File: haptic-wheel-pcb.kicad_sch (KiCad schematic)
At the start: 2 parts, among them J1 Screw_Terminal_01x02, J2 Screw_Terminal_01x02

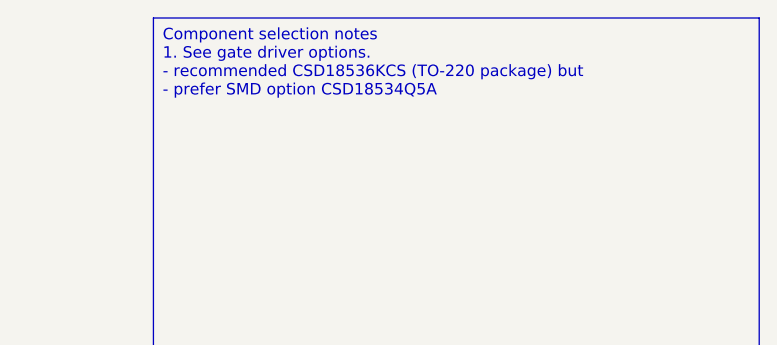
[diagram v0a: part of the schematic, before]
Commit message: routed motor driver fets and shunts
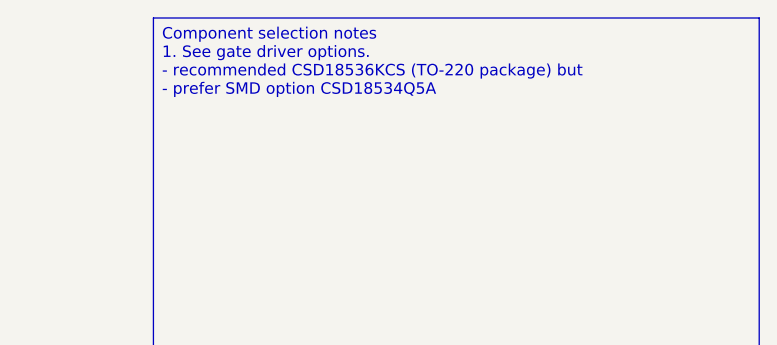
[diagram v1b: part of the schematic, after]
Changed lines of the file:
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@@
 (kicad_sch
-	(version 20231120)
+	(version 20250114)
 	(generator "eeschema")
-	(generator_version "8.0")
+	(generator_version "9.0")
 	(paper "A4")
 	(text_box "Component selection notes\n1. See gate driver options. \n  - recommended CSD18536KCS (TO-220 package) but \n  - prefer SMD option CSD18534Q5A\n"
@@
 		(at 308.61 15.24 0)
 		(size 67.31 44.45)
+		(margins 0.9525 0.9525 0.9525 0.9525)
 		(stroke
 			(width 0)
@@
 		(at 0 434.34)
 		(size 297.18 173.99)
+		(exclude_from_sim no)
+		(in_bom yes)
+		(on_board yes)
+		(dnp no)
 		(fields_autoplaced yes)
 		(stroke
@@
 		(at -2.54 642.62)
 		(size 298.45 233.68)
+		(exclude_from_sim no)
+		(in_bom yes)
+		(on_board yes)
+		(dnp no)
 		(fields_autoplaced yes)
 		(stroke
@@
 		(at -1.27 228.6)
 		(size 299.72 180.34)
+		(exclude_from_sim no)
+		(in_bom yes)
+		(on_board yes)
+		(dnp no)
 		(fields_autoplaced yes)
 		(stroke
@@
 		)
 	)
+	(embedded_fonts no)
 )

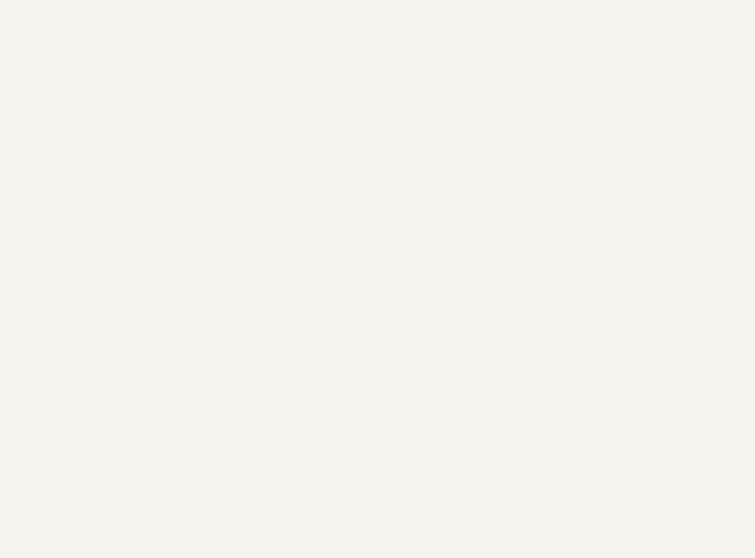
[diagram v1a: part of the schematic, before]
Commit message: route all 3 fets with shunts in a vertical line
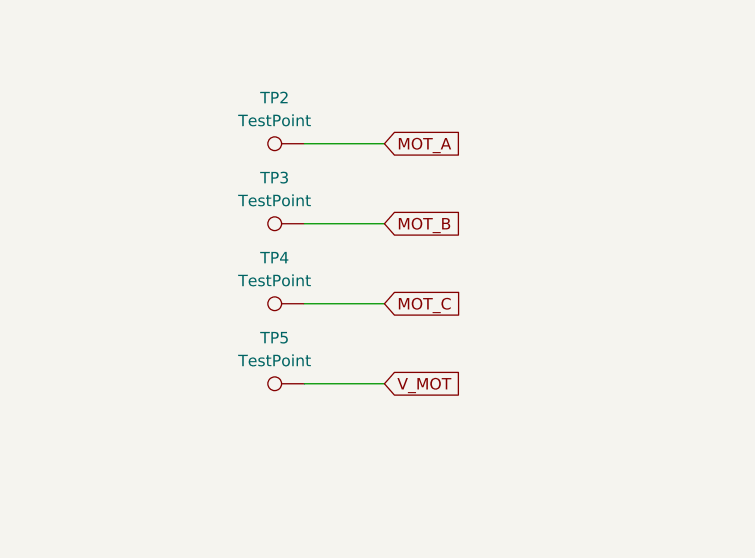
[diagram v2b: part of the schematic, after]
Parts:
- added TP2, TP3, TP4, TP5: TestPoint, TestPoint:TestPoint_Keystone_5019_Miniature, symbol Connector:TestPoint
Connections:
- new net MOT_A: TP2.1
- new net MOT_B: TP3.1
- new net MOT_C: TP4.1
- new net V_MOT: TP5.1

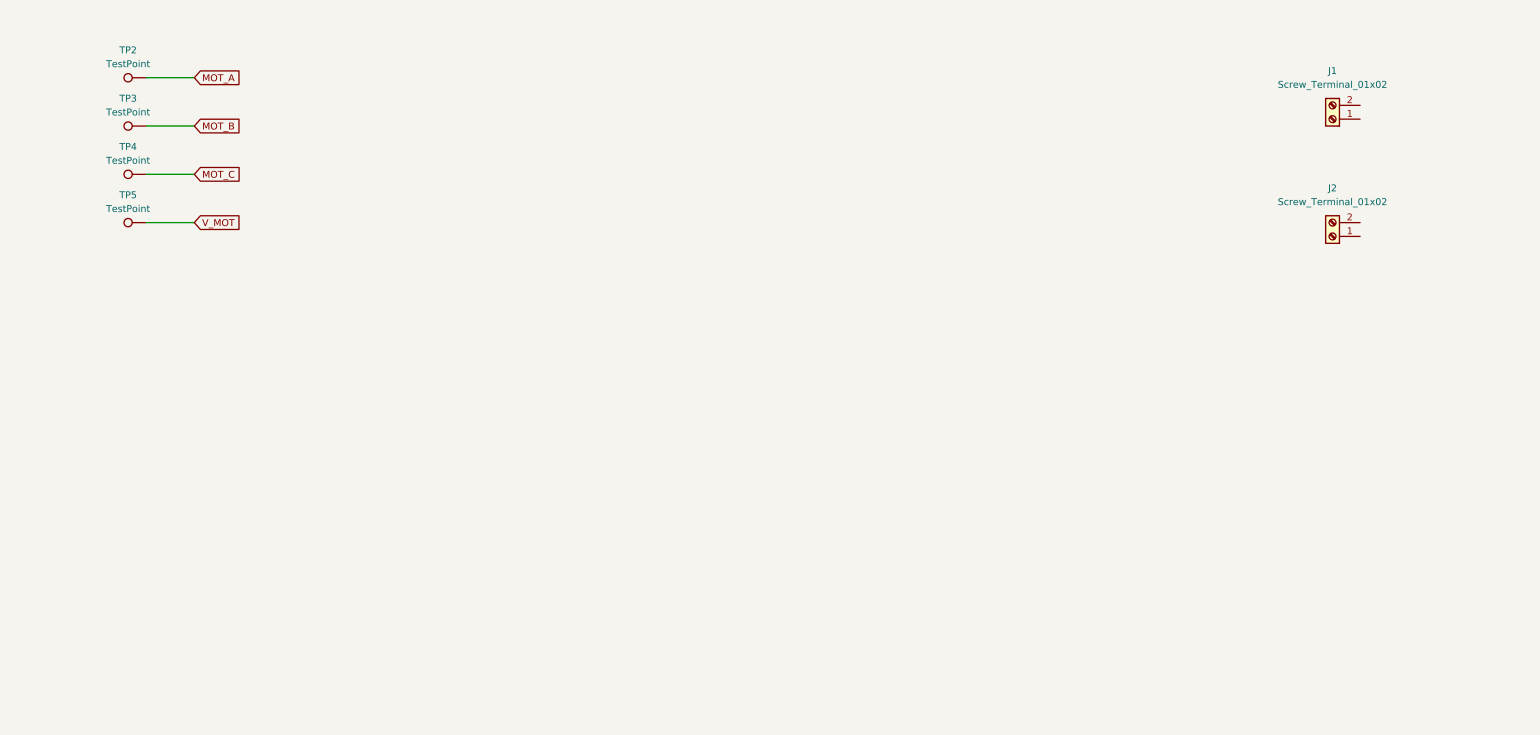
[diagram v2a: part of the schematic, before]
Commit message: selected mcu pins for sense in, SPI
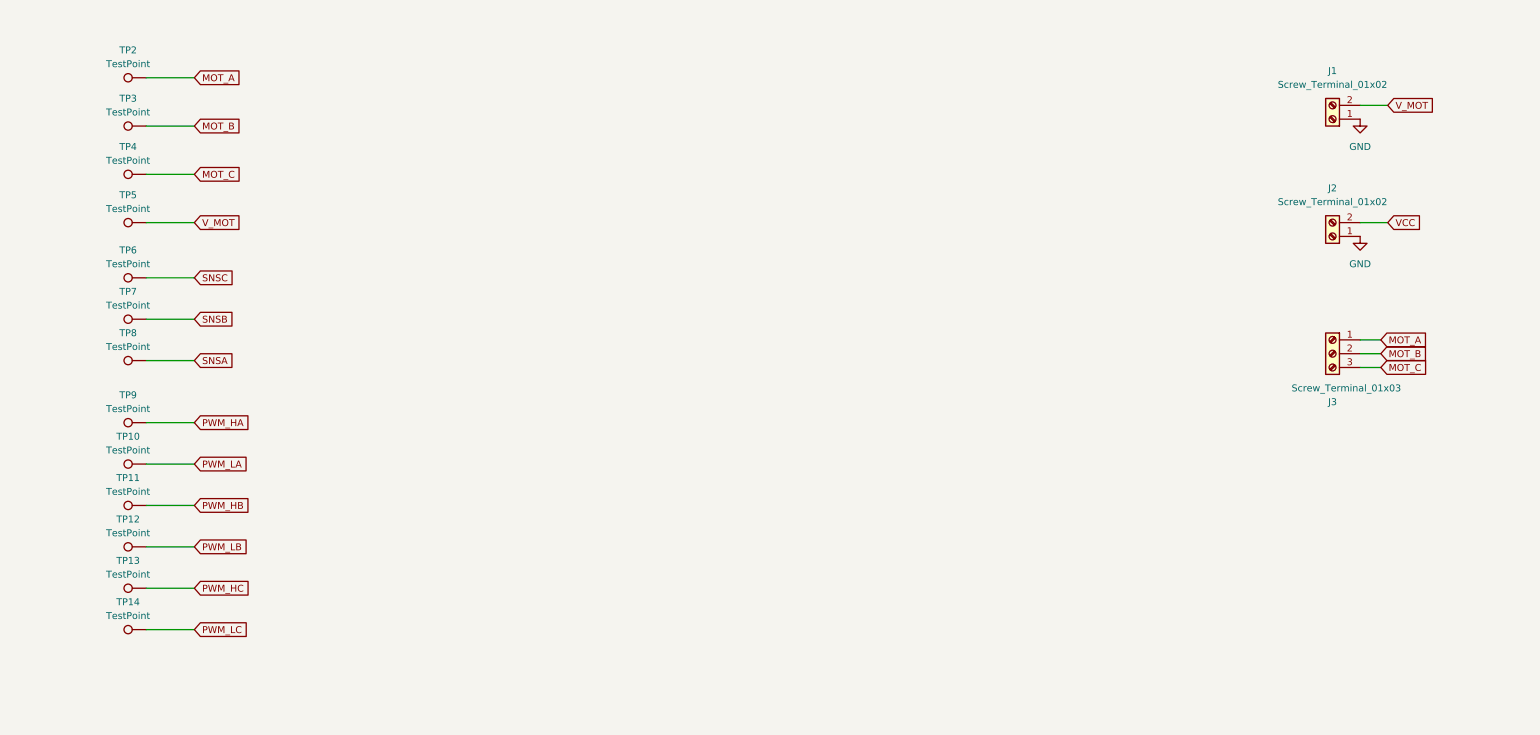
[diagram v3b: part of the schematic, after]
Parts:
- added J3: Screw_Terminal_01x03, TerminalBlock:TerminalBlock_Xinya_XY308-2.54-3P_1x03_P2.54mm_Horizontal, symbol Connector:Screw_Terminal_01x03
- added TP10, TP11, TP12, TP13, TP14, TP6, TP7, TP8, TP9: TestPoint, TestPoint:TestPoint_Keystone_5019_Miniature, symbol Connector:TestPoint
- J1, J2: footprint (none) -> TerminalBlock:TerminalBlock_Xinya_XY308-2.54-2P_1x02_P2.54mm_Horizontal
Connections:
- net MOT_A: now also J3.1 (Pin_1)
- net MOT_B: now also J3.2 (Pin_2)
- net MOT_C: now also J3.3 (Pin_3)
- net V_MOT: now also J1.2 (Pin_2)
- net GND: now reaches J1.1 (Pin_1)
- net GND: now also J2.1 (Pin_1)
- net VCC: now reaches J2.2 (Pin_2)
- new net PWM_HA: TP9.1
- new net PWM_HB: TP11.1
- new net PWM_HC: TP13.1
- new net PWM_LA: TP10.1
- new net PWM_LB: TP12.1
- new net PWM_LC: TP14.1
- new net SNSA: TP8.1
- new net SNSB: TP7.1
- new net SNSC: TP6.1

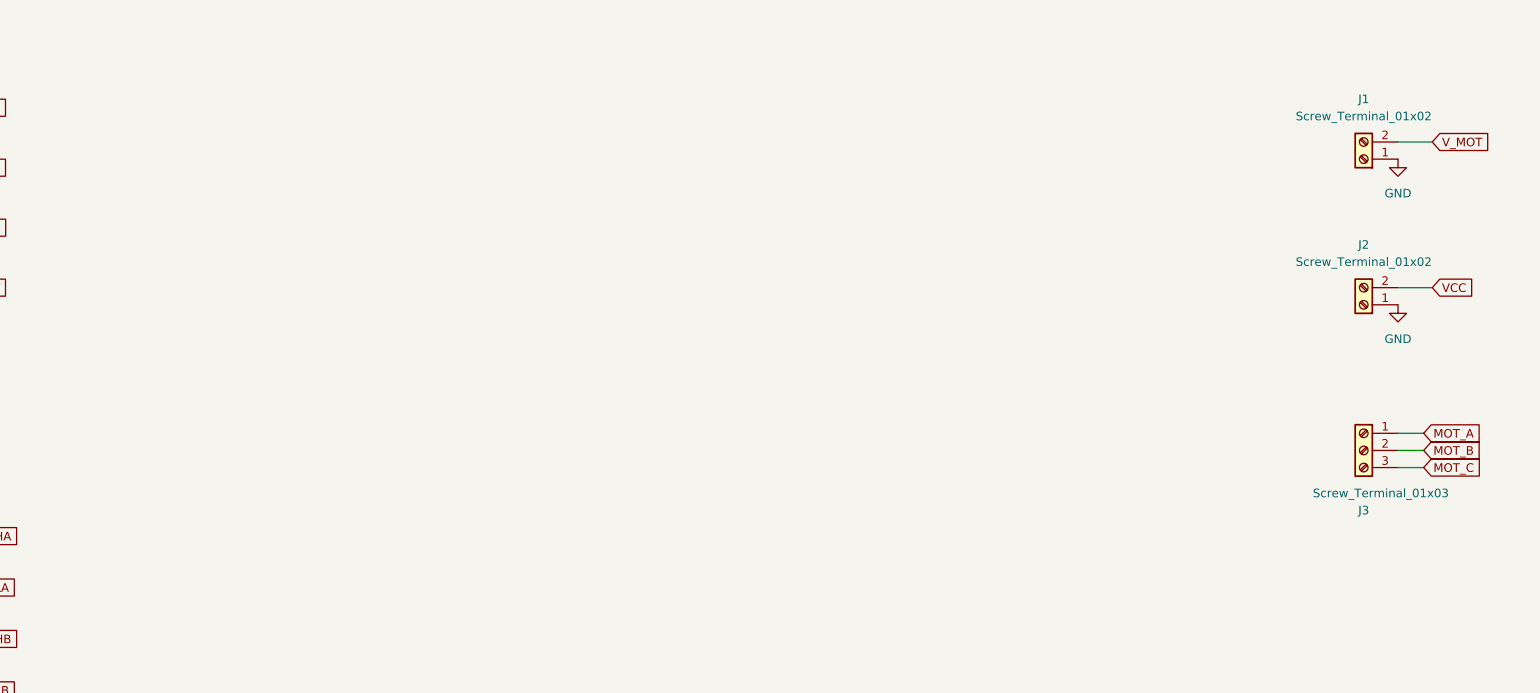
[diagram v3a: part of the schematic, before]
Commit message: big layout - lay pgnd and agnd zones and add SPI header pins
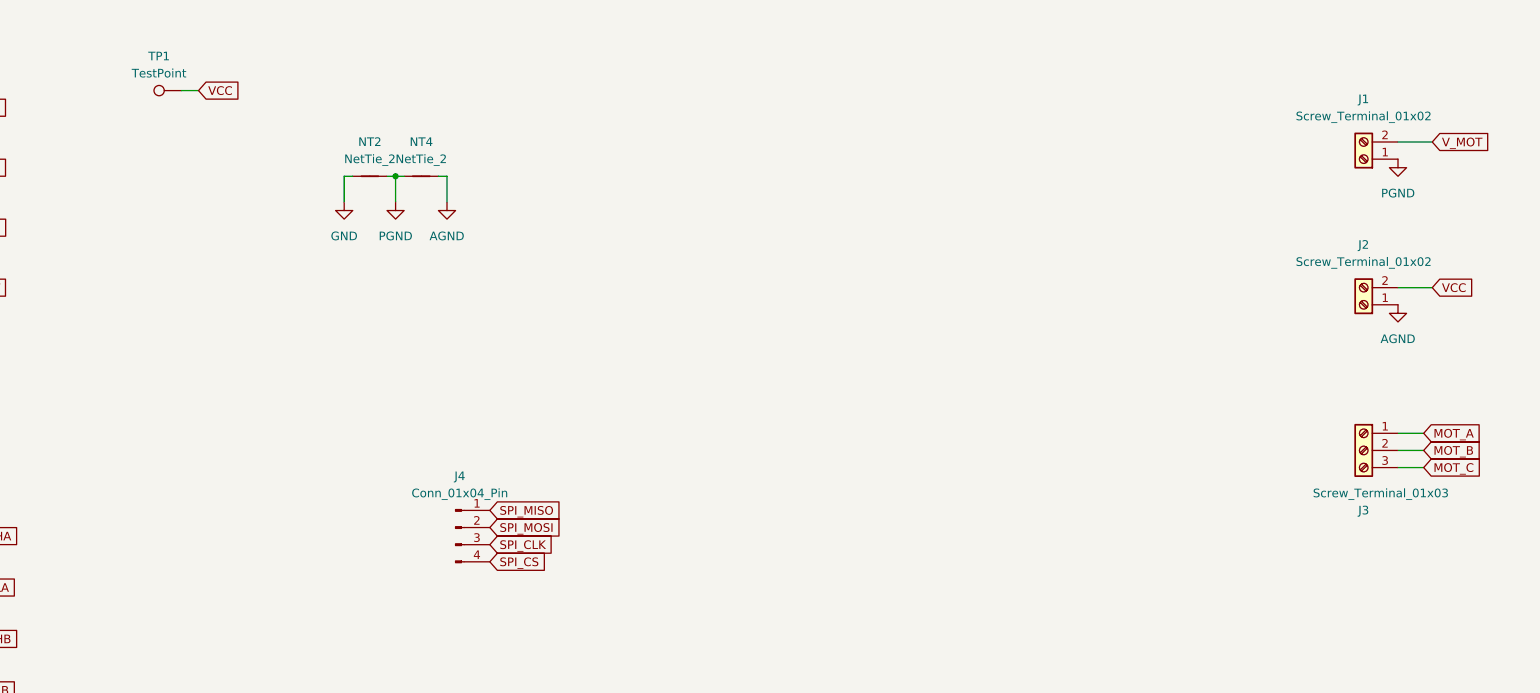
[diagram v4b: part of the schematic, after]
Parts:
- added J4: Conn_01x04_Pin, Connector_PinHeader_2.54mm:PinHeader_1x04_P2.54mm_Vertical, symbol Connector:Conn_01x04_Pin
- added NT2, NT4: NetTie_2, symbol Device:NetTie_2
- added TP1: TestPoint, TestPoint:TestPoint_Keystone_5015_Micro_Mini, symbol Connector:TestPoint
- TP10, TP11, TP12, TP13, TP14, TP2, TP3, TP4, TP5, TP6, TP7, TP8, TP9: footprint TestPoint:TestPoint_Keystone_5019_Miniature -> TestPoint:TestPoint_Keystone_5015_Micro_Mini
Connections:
- net GND: now also NT2.1; no longer J1.1 (Pin_1), J2.1 (Pin_1)
- net VCC: now also TP1.1
- new net AGND: J2.1 (Pin_1), NT4.2
- new net PGND: J1.1 (Pin_1), NT2.2, NT4.1
- new net SPI_CLK: J4.3 (Pin_3)
- new net SPI_CS: J4.4 (Pin_4)
- new net SPI_MISO: J4.1 (Pin_1)
- new net SPI_MOSI: J4.2 (Pin_2)
